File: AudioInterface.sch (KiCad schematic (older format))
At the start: 4 parts, among them J3 REM/DATA, U3 HS-100B

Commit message: Replace 100 uF caps
The ones I had selected before were only rated for 4V, and I need at least 5V (USB bus).
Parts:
- C11: Manufacturer_Part_Number TPST107M004R0500 -> TACT107M006XTA; Price 0.93 -> 4.4; Vendor Part Number 581-TPST107M004R0500 -> 581-TACT107M006XTA
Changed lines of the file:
@@
 F 1 "100μF" H 7165 2005 50 0000 L CNN
 F 2 "Capacitor_SMD:C_1210_3225Metric" H 7088 1900 50 0001 C CNN
-F 3 "https://www.mouser.com/datasheet/2/40/TPS-2066671.pdf" H 7050 2050 50 0001 C CNN
+F 3 "https://www.mouser.com/datasheet/2/40/tac-776418.pdf" H 7050 2050 50 0001 C CNN
 F 4 "AVX" H 7165 2196 50 0001 C CNN "Manufacturer_Name"
-F 5 "TPST107M004R0500" H 7165 2196 50 0001 C CNN "Manufacturer_Part_Number"
-F 6 "0.93" H 7165 2196 50 0001 C CNN "Price"
-F 7 "581-TPST107M004R0500" H 7165 2196 50 0001 C CNN "Vendor Part Number"
+F 5 "TACT107M006XTA" H 7165 2196 50 0001 C CNN "Manufacturer_Part_Number"
+F 6 "4.4" H 7165 2196 50 0001 C CNN "Price"
+F 7 "581-TACT107M006XTA" H 7165 2196 50 0001 C CNN "Vendor Part Number"
 F 8 "Mouser" H 7165 2196 50 0001 C CNN "Vendor"
 	1    7050 2050

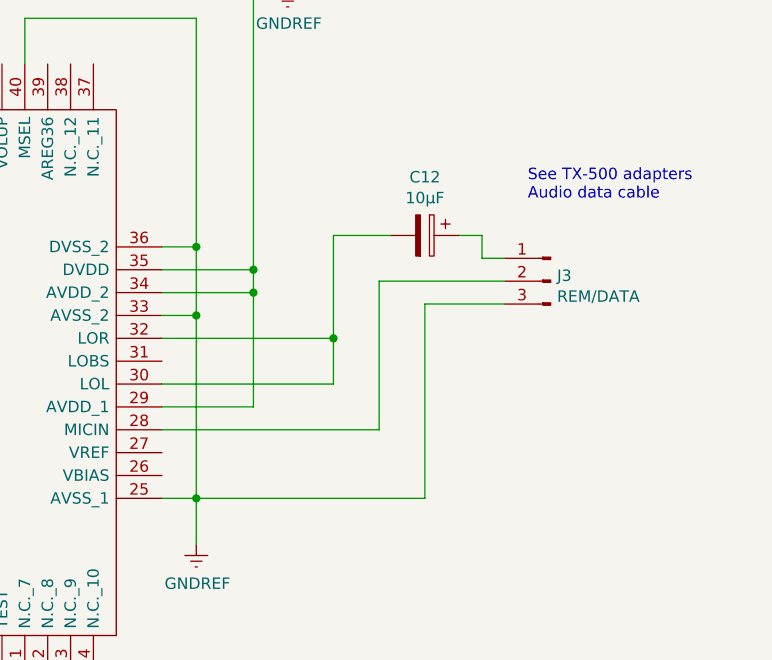
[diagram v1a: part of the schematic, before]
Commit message: Add a 15mm buffer for the GX12 bulkhead connectors
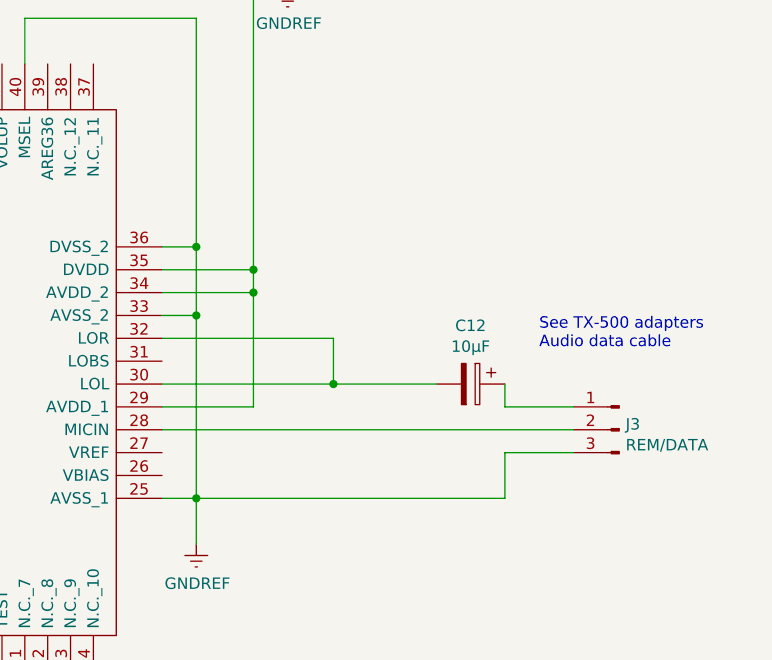
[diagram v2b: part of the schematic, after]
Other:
- moved on the sheet: C12, J3
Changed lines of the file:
@@
 U 1 1 605AF753
 P 4800 3350
-AR Path="/605AF753" Ref="IC?" Part="1"
-AR Path="/605AB33C/605AF753" Ref="U3" Part="1"
-F 0 "U3" H 4600 3800 50 0000 L CNN
-F 1 "HS-100B" H 4500 3700 50 0000 L CNN
-F 2 "Package_QFP:LQFP-48_7x7mm_P0.5mm" H 6350 3950 50 0001 L CNN
-F 3 "1.6" H 6350 3850 50 0001 L CNN
-F 4 "USB Audio Interface" H 6350 3750 50 0001 L CNN "Description"
-F 5 "1.6" H 6350 3650 50 0001 L CNN "Height"
-F 6 "Cmedia" H 6350 3550 50 0001 L CNN "Manufacturer_Name"
-F 7 "HS-100B" H 6350 3450 50 0001 L CNN "Manufacturer_Part_Number"
-F 8 "0.78" H 4600 3900 50 0001 C CNN "Price"
-F 9 "HS-100B" H 4600 3900 50 0001 C CNN "Vendor Part Number"
-F 10 "Symmetry" H 4600 3900 50 0001 C CNN "Vendor"
+AR Path="/605AF753" Ref="IC?"  Part="1"
+AR Path="/605AB33C/605AF753" Ref="U3"  Part="1"
+F 0 "U3" H 4600 3800 50  0000 L CNN
+F 1 "HS-100B" H 4500 3700 50  0000 L CNN
+F 2 "Package_QFP:LQFP-48_7x7mm_P0.5mm" H 6350 3950 50  0001 L CNN
+F 3 "1.6" H 6350 3850 50  0001 L CNN
+F 4 "USB Audio Interface" H 6350 3750 50  0001 L CNN "Description"
+F 5 "1.6" H 6350 3650 50  0001 L CNN "Height"
+F 6 "Cmedia" H 6350 3550 50  0001 L CNN "Manufacturer_Name"
+F 7 "HS-100B" H 6350 3450 50  0001 L CNN "Manufacturer_Part_Number"
+F 8 "0.78" H 4600 3900 50  0001 C CNN "Price"
+F 9 "HS-100B" H 4600 3900 50  0001 C CNN "Vendor Part Number"
+F 10 "Symmetry" H 4600 3900 50  0001 C CNN "Vendor"
 	1    4800 3350
 	1    0    0    -1
@@
 L Connector:Conn_01x03_Male J?
 U 1 1 605AF759
-P 8200 3500
-AR Path="/605AF759" Ref="J?" Part="1"
-AR Path="/605AB33C/605AF759" Ref="J3" Part="1"
-F 0 "J3" H 8172 3524 50 0000 R CNN
-F 1 "REM/DATA" H 8172 3433 50 0000 R CNN
-F 2 "Connector_JST:JST_PH_B3B-PH-SM4-TB_1x03-1MP_P2.00mm_Vertical" H 8200 3500 50 0001 C CNN
-F 3 "https://www.mouser.com/datasheet/2/737/4389_C13924-001_CCP-W20-03-BK-SMT-R-A-1708610.pdf" H 8200 3500 50 0001 C CNN
-F 4 "TX-500 REM/DATA Interconnect" H 8172 3624 50 0001 C CNN "Description"
-F 5 "JST" H 8172 3624 50 0001 C CNN "Manufacturer_Name"
-F 6 "B3B-PH-SM4-TB" H 8172 3624 50 0001 C CNN "Manufacturer_Part_Number"
-F 7 "0.35" H 8172 3624 50 0001 C CNN "Price"
-F 8 "485-4389" H 8172 3624 50 0001 C CNN "Vendor Part Number"
-F 9 "Mouser" H 8172 3624 50 0001 C CNN "Vendor"
-	1    8200 3500
+P 8500 4150
+AR Path="/605AF759" Ref="J?"  Part="1"
+AR Path="/605AB33C/605AF759" Ref="J3"  Part="1"
+F 0 "J3" H 8472 4174 50  0000 R CNN
+F 1 "REM/DATA" H 8472 4083 50  0000 R CNN
+F 2 "Connector_JST:JST_PH_B3B-PH-SM4-TB_1x03-1MP_P2.00mm_Vertical" H 8500 4150 50  0001 C CNN
+F 3 "https://www.mouser.com/datasheet/2/737/4389_C13924-001_CCP-W20-03-BK-SMT-R-A-1708610.pdf" H 8500 4150 50  0001 C CNN
+F 4 "TX-500 REM/DATA Interconnect" H 8472 4274 50  0001 C CNN "Description"
+F 5 "JST" H 8472 4274 50  0001 C CNN "Manufacturer_Name"
+F 6 "B3B-PH-SM4-TB" H 8472 4274 50  0001 C CNN "Manufacturer_Part_Number"
+F 7 "0.35" H 8472 4274 50  0001 C CNN "Price"
+F 8 "485-4389" H 8472 4274 50  0001 C CNN "Vendor Part Number"
+F 9 "Mouser" H 8472 4274 50  0001 C CNN "Vendor"
+	1    8500 4150
 	-1   0    0    -1
 $EndComp
@@
 U 1 1 604B503B
 P 6650 4650
-F 0 "#PWR0110" H 6650 4400 50 0001 C CNN
-F 1 "GNDREF" H 6655 4477 50 0000 C CNN
-F 2 "" H 6650 4650 50 0001 C CNN
-F 3 "" H 6650 4650 50 0001 C CNN
+F 0 "#PWR0110" H 6650 4400 50  0001 C CNN
+F 1 "GNDREF" H 6655 4477 50  0000 C CNN
+F 2 "" H 6650 4650 50  0001 C CNN
+F 3 "" H 6650 4650 50  0001 C CNN
 	1    6650 4650
 	1    0    0    -1
@@
 U 1 1 604B77F8
 P 4600 5500
-F 0 "#PWR0111" H 4600 5250 50 0001 C CNN
-F 1 "GNDREF" H 4605 5327 50 0000 C CNN
-F 2 "" H 4600 5500 50 0001 C CNN
-F 3 "" H 4600 5500 50 0001 C CNN
+F 0 "#PWR0111" H 4600 5250 50  0001 C CNN
+F 1 "GNDREF" H 4605 5327 50  0000 C CNN
+F 2 "" H 4600 5500 50  0001 C CNN
+F 3 "" H 4600 5500 50  0001 C CNN
 	1    4600 5500
 	1    0    0    -1
@@
 U 1 1 604B97A3
 P 6900 1800
-F 0 "#PWR0112" H 6900 1650 50 0001 C CNN
-F 1 "VBUS" H 6915 1973 50 0000 C CNN
-F 2 "" H 6900 1800 50 0001 C CNN
-F 3 "" H 6900 1800 50 0001 C CNN
+F 0 "#PWR0112" H 6900 1650 50  0001 C CNN
+F 1 "VBUS" H 6915 1973 50  0000 C CNN
+F 2 "" H 6900 1800 50  0001 C CNN
+F 3 "" H 6900 1800 50  0001 C CNN
 	1    6900 1800
 	1    0    0    -1
@@
 L Device:CP C12
 U 1 1 604CC1E1
-P 7650 3300
-F 0 "C12" V 7395 3300 50 0000 C CNN
-F 1 "10μF" V 7486 3300 50 0000 C CNN
-F 2 "Capacitor_SMD:C_1210_3225Metric" H 7688 3150 50 0001 C CNN
-F 3 "https://www.mouser.com/datasheet/2/210/WTC_MLCC_General_Purpose-1534899.pdf" H 7650 3300 50 0001 C CNN
-F 4 "Walsin" H 7395 3400 50 0001 C CNN "Manufacturer_Name"
-F 5 "1210F106Z100CT" H 7395 3400 50 0001 C CNN "Manufacturer_Part_Number"
-F 6 "0.29" H 7395 3400 50 0001 C CNN "Price"
-F 7 "791-1210F106Z100CT" H 7395 3400 50 0001 C CNN "Vendor Part Number"
-F 8 "Mouser" H 7395 3400 50 0001 C CNN "Vendor"
-	1    7650 3300
+P 7850 3950
+F 0 "C12" V 7595 3950 50  0000 C CNN
+F 1 "10μF" V 7686 3950 50  0000 C CNN
+F 2 "Capacitor_SMD:C_1210_3225Metric" H 7888 3800 50  0001 C CNN
+F 3 "https://www.mouser.com/datasheet/2/210/WTC_MLCC_General_Purpose-1534899.pdf" H 7850 3950 50  0001 C CNN
+F 4 "Walsin" H 7595 4050 50  0001 C CNN "Manufacturer_Name"
+F 5 "1210F106Z100CT" H 7595 4050 50  0001 C CNN "Manufacturer_Part_Number"
+F 6 "0.29" H 7595 4050 50  0001 C CNN "Price"
+F 7 "791-1210F106Z100CT" H 7595 4050 50  0001 C CNN "Vendor Part Number"
+F 8 "Mouser" H 7595 4050 50  0001 C CNN "Vendor"
+	1    7850 3950
 	0    1    1    0
 $EndComp
@@
 U 1 1 605433B2
 P 7050 2050
-F 0 "C11" H 7165 2096 50 0000 L CNN
-F 1 "100μF" H 7165 2005 50 0000 L CNN
-F 2 "Capacitor_SMD:C_1210_3225Metric" H 7088 1900 50 0001 C CNN
-F 3 "https://www.mouser.com/datasheet/2/40/tac-776418.pdf" H 7050 2050 50 0001 C CNN
-F 4 "AVX" H 7165 2196 50 0001 C CNN "Manufacturer_Name"
-F 5 "TACT107M006XTA" H 7165 2196 50 0001 C CNN "Manufacturer_Part_Number"
-F 6 "4.4" H 7165 2196 50 0001 C CNN "Price"
-F 7 "581-TACT107M006XTA" H 7165 2196 50 0001 C CNN "Vendor Part Number"
-F 8 "Mouser" H 7165 2196 50 0001 C CNN "Vendor"
+F 0 "C11" H 7165 2096 50  0000 L CNN
+F 1 "100μF" H 7165 2005 50  0000 L CNN
+F 2 "Capacitor_SMD:C_1210_3225Metric" H 7088 1900 50  0001 C CNN
+F 3 "https://www.mouser.com/datasheet/2/40/tac-776418.pdf" H 7050 2050 50  0001 C CNN
+F 4 "AVX" H 7165 2196 50  0001 C CNN "Manufacturer_Name"
+F 5 "TACT107M006XTA" H 7165 2196 50  0001 C CNN "Manufacturer_Part_Number"
+F 6 "4.4" H 7165 2196 50  0001 C CNN "Price"
+F 7 "581-TACT107M006XTA" H 7165 2196 50  0001 C CNN "Vendor Part Number"
+F 8 "Mouser" H 7165 2196 50  0001 C CNN "Vendor"
 	1    7050 2050
 	1    0    0    -1
@@
 U 1 1 60544A17
 P 7050 2200
-F 0 "#PWR0129" H 7050 1950 50 0001 C CNN
-F 1 "GNDREF" H 7055 2027 50 0000 C CNN
-F 2 "" H 7050 2200 50 0001 C CNN
-F 3 "" H 7050 2200 50 0001 C CNN
+F 0 "#PWR0129" H 7050 1950 50  0001 C CNN
+F 1 "GNDREF" H 7055 2027 50  0000 C CNN
+F 2 "" H 7050 2200 50  0001 C CNN
+F 3 "" H 7050 2200 50  0001 C CNN
 	1    7050 2200
 	1    0    0    -1
@@
 Text Notes 5400 1700 0    50   ~ 0
 See HS-100B datasheet
-Text Notes 8100 3150 0    50   ~ 0
+Text Notes 8150 3800 0    50   ~ 0
 See TX-500 adapters\nAudio data cable
 Text HLabel 5600 2200 1    50   Input ~ 0
@@
 	4800 4450 4600 4450
 Wire Wire Line
-	6500 4150 7450 4150
-Wire Wire Line
-	7450 4150 7450 3500
-Wire Wire Line
-	7450 3500 8000 3500
-Wire Wire Line
 	6500 3950 7250 3950
 Wire Wire Line
@@
 Wire Wire Line
 	6650 2350 6650 3350
-Wire Wire Line
-	7250 3300 7500 3300
-Wire Wire Line
-	7250 3300 7250 3750
-Wire Wire Line
-	7800 3300 7900 3300
-Wire Wire Line
-	7900 3300 7900 3400
-Wire Wire Line
-	7900 3400 8000 3400
-Wire Wire Line
-	8000 3600 7650 3600
-Wire Wire Line
-	7650 3600 7650 4450
-Wire Wire Line
-	7650 4450 6650 4450
 Wire Wire Line
 	7050 1900 6900 1900
@@
 Connection ~ 6650 3650
 Connection ~ 6650 4450
-Connection ~ 7250 3750
 Connection ~ 6900 3550
 Connection ~ 4600 5400
@@
 Connection ~ 6900 1900
 Connection ~ 6900 3450
+Wire Wire Line
+	8000 3950 8000 4050
+Wire Wire Line
+	8000 4050 8300 4050
+Wire Wire Line
+	8000 4450 8000 4250
+Wire Wire Line
+	8000 4250 8300 4250
+Wire Wire Line
+	7250 3950 7700 3950
+Connection ~ 7250 3950
+Wire Wire Line
+	6500 4150 8300 4150
+Wire Wire Line
+	6650 4450 8000 4450
 $EndSCHEMATC

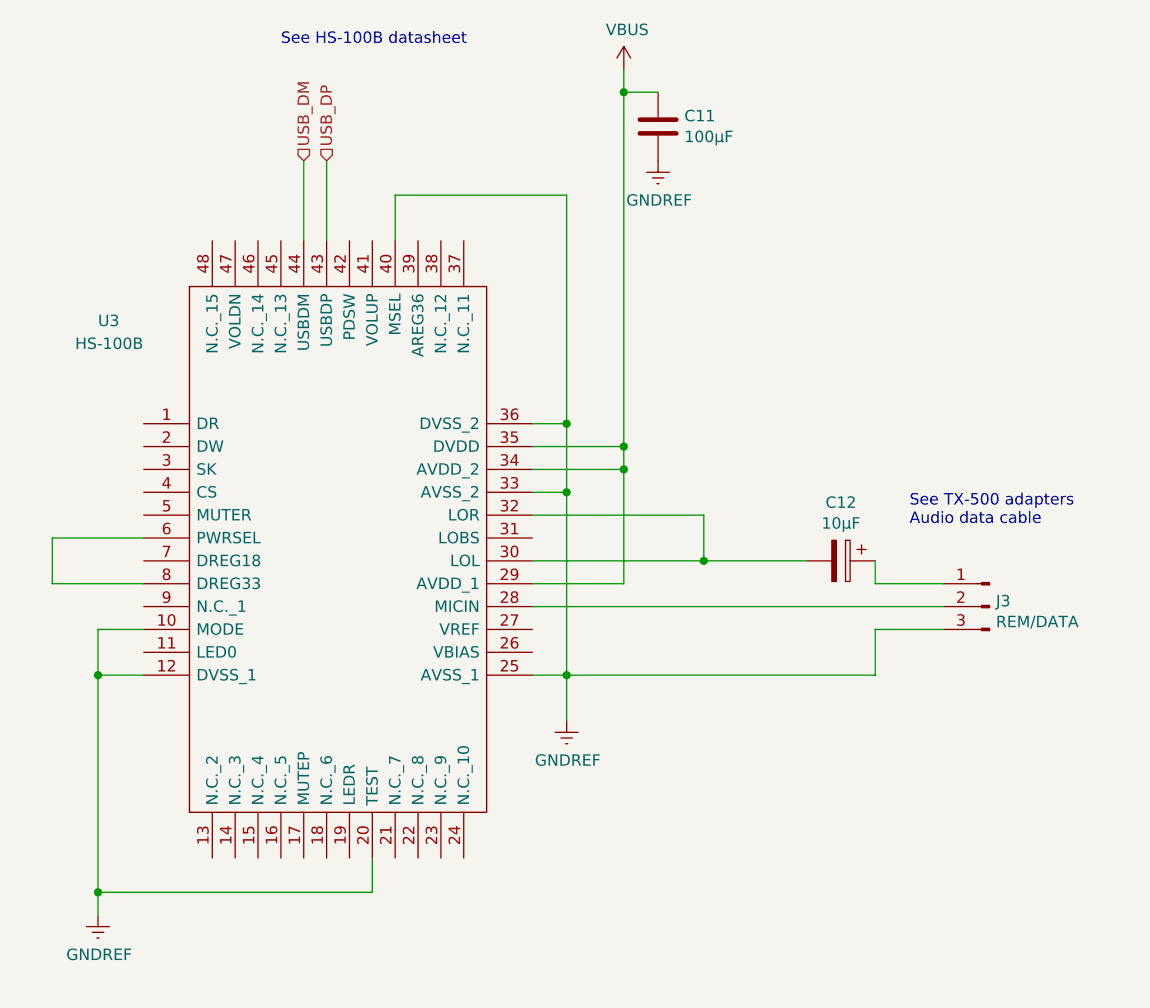
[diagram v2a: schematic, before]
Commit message: Add ID markings on schema and pcb
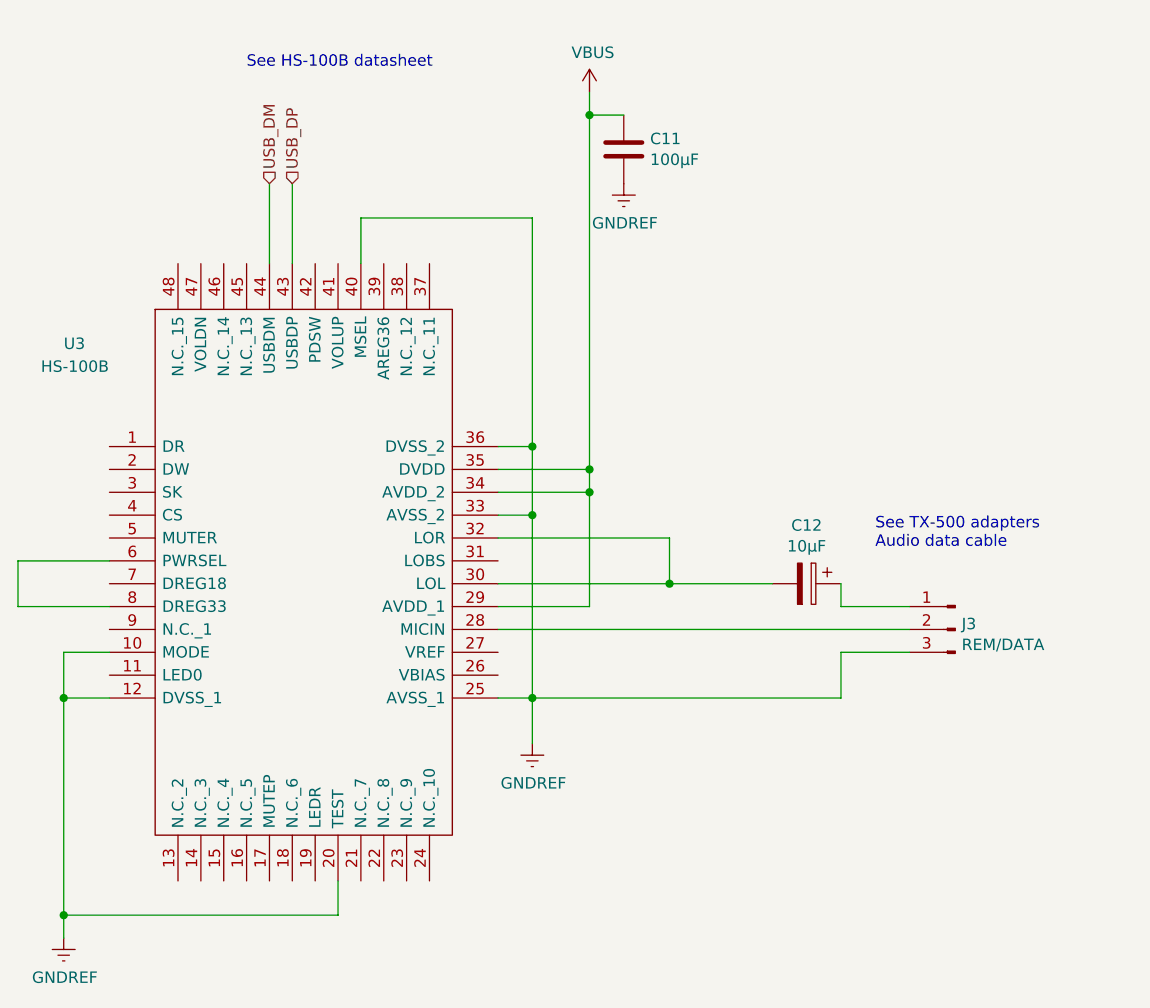
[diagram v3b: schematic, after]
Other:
- moved on the sheet: C11, C12, J3, U3
